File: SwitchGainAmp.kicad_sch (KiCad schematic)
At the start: 22 parts, among them Q3 BSS138, Q4 BSS138, Q5 BSS138, Q6 BSS138, U8 LT1493

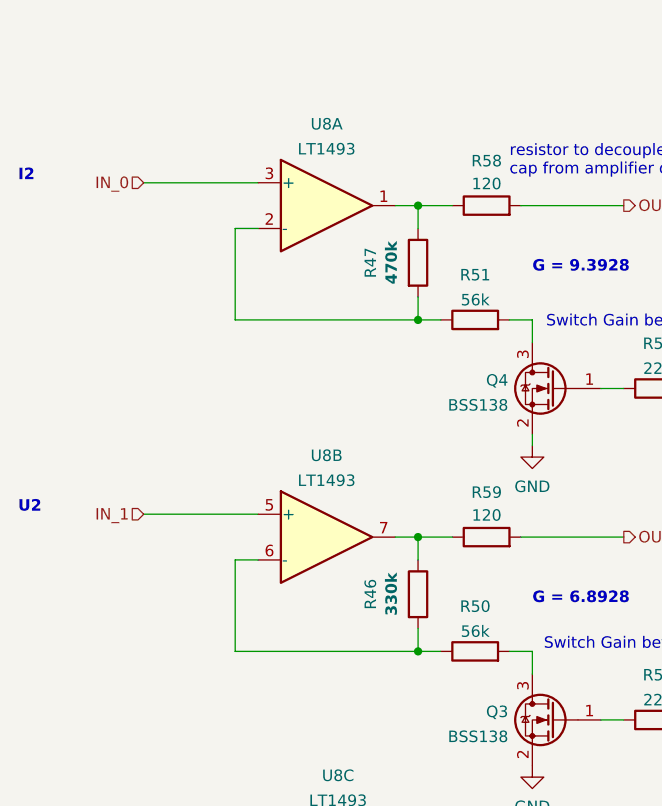
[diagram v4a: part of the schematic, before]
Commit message: updated channel numbering
changed CH2 into CH0 to match software
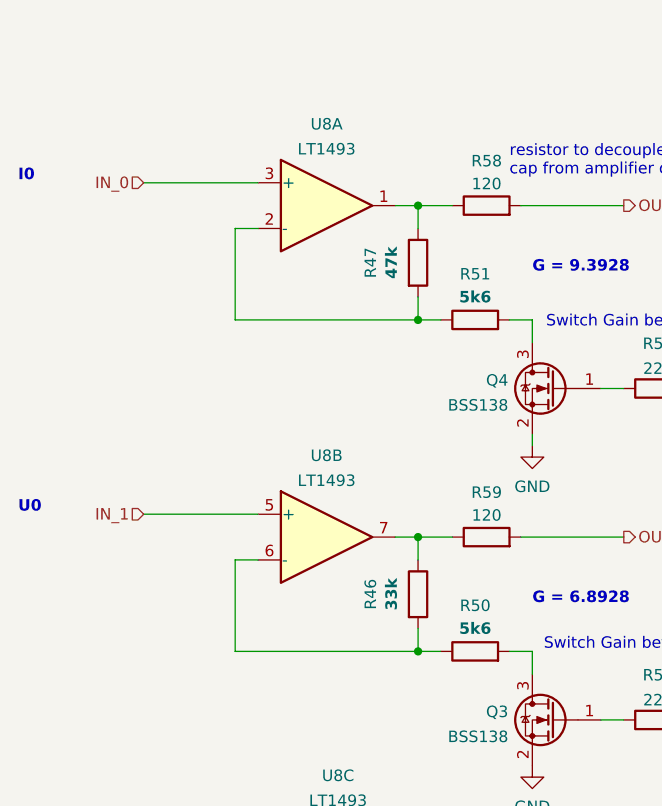
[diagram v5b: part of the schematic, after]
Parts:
- R46: value 330k -> 33k
- R47: value 470k -> 47k
- R50, R51: value 56k -> 5k6
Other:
- note added: "I0"
- note added: "U0"
- note removed: "I2"
- note removed: "U2"
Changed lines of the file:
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@@
     (effects (font (size 1.27 1.27) bold) (justify left bottom))
   )
-  (text "U2" (at 48.26 73.66 0)
+  (text "U0" (at 48.26 73.66 0)
     (effects (font (size 1.27 1.27) bold) (justify left bottom))
   )
@@
     (effects (font (size 1.27 1.27) bold) (justify left bottom))
   )
-  (text "I2" (at 48.26 36.83 0)
+  (text "I0" (at 48.26 36.83 0)
     (effects (font (size 1.27 1.27) (thickness 0.254) bold) (justify left bottom))
   )
@@
   (symbol (lib_id "Device:R") (at 99.06 88.9 90) (unit 1)
     (in_bom yes) (on_board yes) (dnp no) (fields_autoplaced)
-    (property "Reference" "R50" (at 99.06 83.9175 90)
-      (effects (font (size 1.27 1.27)))
-    )
-    (property "Value" "56k" (at 99.06 86.6926 90)
-      (effects (font (size 1.27 1.27)))
+    (property "Reference" "R50" (at 99.06 83.82 90)
+      (effects (font (size 1.27 1.27)))
+    )
+    (property "Value" "5k6" (at 99.06 86.36 90)
+      (effects (font (size 1.27 1.27) bold))
     )
     (property "Footprint" "Resistor_SMD:R_0603_1608Metric" (at 99.06 90.678 90)
@@
       (effects (font (size 1.27 1.27)))
     )
-    (property "Value" "330k" (at 89.7636 82.55 90)
+    (property "Value" "33k" (at 89.7636 82.55 90)
       (effects (font (size 1.27 1.27) bold))
     )
@@
       (effects (font (size 1.27 1.27)))
     )
-    (property "Value" "470k" (at 89.7636 45.72 90)
+    (property "Value" "47k" (at 89.7636 45.72 90)
       (effects (font (size 1.27 1.27) bold))
     )
@@
   (symbol (lib_id "Device:R") (at 99.06 52.07 90) (unit 1)
     (in_bom yes) (on_board yes) (dnp no) (fields_autoplaced)
-    (property "Reference" "R51" (at 99.06 47.0875 90)
-      (effects (font (size 1.27 1.27)))
-    )
-    (property "Value" "56k" (at 99.06 49.8626 90)
-      (effects (font (size 1.27 1.27)))
+    (property "Reference" "R51" (at 99.06 46.99 90)
+      (effects (font (size 1.27 1.27)))
+    )
+    (property "Value" "5k6" (at 99.06 49.53 90)
+      (effects (font (size 1.27 1.27) bold))
     )
     (property "Footprint" "Resistor_SMD:R_0603_1608Metric" (at 99.06 53.848 90)

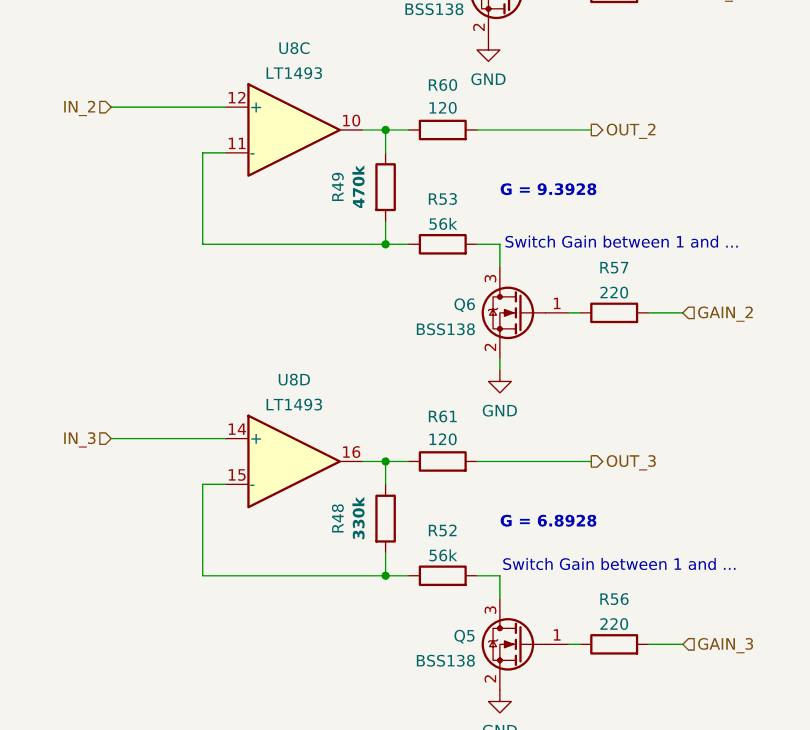
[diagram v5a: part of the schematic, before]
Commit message: updated gain setting resistors of channel 1
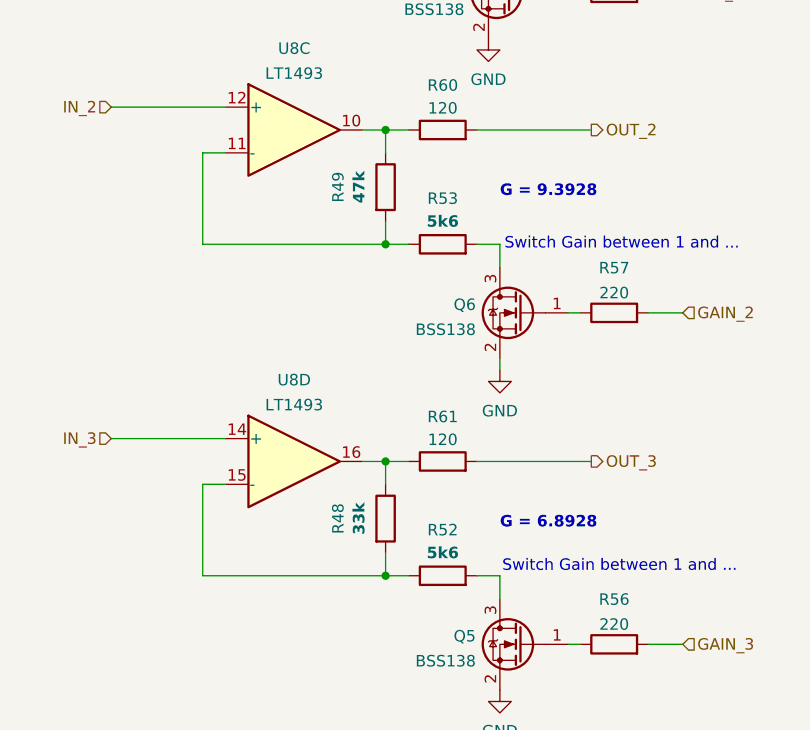
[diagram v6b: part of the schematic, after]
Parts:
- R48: value 330k -> 33k
- R49: value 470k -> 47k
- R52, R53: value 56k -> 5k6
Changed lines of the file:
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@@
   (symbol (lib_id "Device:R") (at 100.33 124.46 90) (unit 1)
     (in_bom yes) (on_board yes) (dnp no) (fields_autoplaced)
-    (property "Reference" "R53" (at 100.33 119.4775 90)
-      (effects (font (size 1.27 1.27)))
-    )
-    (property "Value" "56k" (at 100.33 122.2526 90)
-      (effects (font (size 1.27 1.27)))
+    (property "Reference" "R53" (at 100.33 119.38 90)
+      (effects (font (size 1.27 1.27)))
+    )
+    (property "Value" "5k6" (at 100.33 121.92 90)
+      (effects (font (size 1.27 1.27) bold))
     )
     (property "Footprint" "Resistor_SMD:R_0603_1608Metric" (at 100.33 126.238 90)
@@
   (symbol (lib_id "Device:R") (at 100.33 161.29 90) (unit 1)
     (in_bom yes) (on_board yes) (dnp no) (fields_autoplaced)
-    (property "Reference" "R52" (at 100.33 156.3075 90)
-      (effects (font (size 1.27 1.27)))
-    )
-    (property "Value" "56k" (at 100.33 159.0826 90)
-      (effects (font (size 1.27 1.27)))
+    (property "Reference" "R52" (at 100.33 156.21 90)
+      (effects (font (size 1.27 1.27)))
+    )
+    (property "Value" "5k6" (at 100.33 158.75 90)
+      (effects (font (size 1.27 1.27) bold))
     )
     (property "Footprint" "Resistor_SMD:R_0603_1608Metric" (at 100.33 163.068 90)
@@
       (effects (font (size 1.27 1.27)))
     )
-    (property "Value" "470k" (at 91.0336 118.11 90)
+    (property "Value" "47k" (at 91.0336 118.11 90)
       (effects (font (size 1.27 1.27) bold))
     )
@@
       (effects (font (size 1.27 1.27)))
     )
-    (property "Value" "330k" (at 91.0336 154.94 90)
+    (property "Value" "33k" (at 91.0336 154.94 90)
       (effects (font (size 1.27 1.27) bold))
     )
